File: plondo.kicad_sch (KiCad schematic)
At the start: 31 parts, among them J1 AVR ISP, J2 USB4085, U1 ATmega32A-P, Y1 16MHz

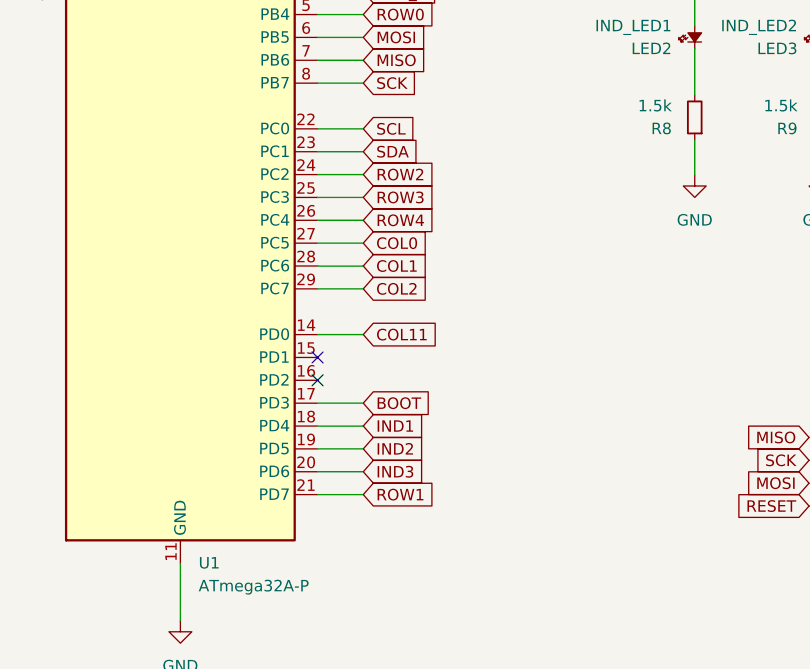
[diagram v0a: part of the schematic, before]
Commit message: complete connecting key matrix
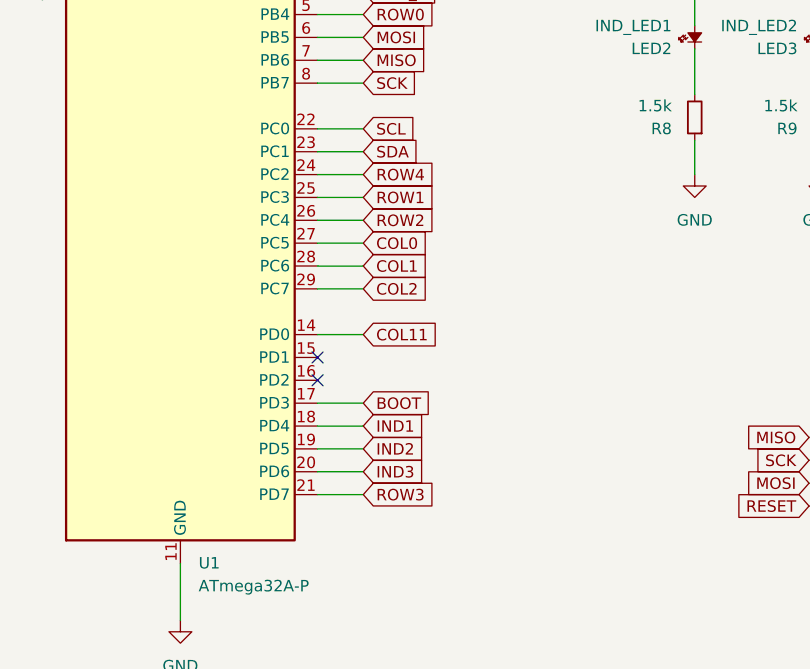
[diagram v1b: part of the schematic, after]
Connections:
- net ROW1: now also U1.25 (PC3); no longer U1.21 (PD7)
- net ROW2: now also U1.26 (PC4); no longer U1.24 (PC2)
- net ROW3: now also U1.21 (PD7); no longer U1.25 (PC3)
- net ROW4: now also U1.24 (PC2); no longer U1.26 (PC4)
